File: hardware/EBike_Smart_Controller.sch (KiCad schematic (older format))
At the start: 18 parts

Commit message: More work on schematic: added connections to Zero LPC2103 board.
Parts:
- added P3: Zero LPC2103 board, symbol CONN_20X2
- added P4: BLUETOOTH_MODULE, symbol BLUETOOTH_MODULE
- C1, C3, C4: renamed from C?; value 100nF -> 10nF
- gave numbers to parts that had none: 15
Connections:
- net labels added: UART RX (LPC2103 P0.1), UART TX (LPC2103 P0.0)
- wire segments 63 -> 71
- no-connect marks 0 -> 59
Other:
- note added: "ERROR: needs conversion from 5V to 3.3V!!"

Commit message: This may be a final version of the schematic.
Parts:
- added P5, P6: CONN_10, symbol CONN_10
- added R11: 2K2, symbol R_MINI
- added R12, R13, R14, R15, R16, R17: 3K6, symbol R_MINI
- R10, R8, R9: value 10K -> 2K2
- R2, R4: value 3K6 -> 3K6 1%
- R3, R5: value 6K8 -> 6K8 1%
- R6: value 100K -> 100K 1%
- R7: value 10K -> 10K 1%
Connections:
- net labels added: IO for mosfet phase_a low (LPC2103 P0.7), IO for mosfet phase_b low (LPC2103 P0.8), IO for mosfet phase_c low (LPC2103 P0.9), PWM for mosfet phase_a high (LPC2103 P0.12), PWM for mosfet phase_b high (LPC2103 P0.13), PWM for mosfet phase_c high (LPC2103 P0.19)
- wire segments 71 -> 123
- no-connect marks 59 -> 55
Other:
- note added: "(C28)"
- note added: "(CPU1)"
- note added: "(CPU2)"
- note added: "(CPU3)"
- note added: "(CPU32)"
- note added: "(CPU33)"
- note added: "(CPU4)"
- note added: "(CPU44)"
- note added: "(CPU5)"
- note added: "(R50)"
- note added: "(R55)"
- note added: "(R56)"
- note added: "EBike Smart Controller main board"
- note added: "KU63 controller"
- note added: "Note: 3V3 power\nsource is from\nZero LPC2103\nboard."
- note added: "Note: 5V power source is from KU63 controller."
- note added: "Note: LPC2103 pins are 5V tolerant."
- note added: "Note: exchange R46 (shunt resistor) by this current sensor IC."
- note added: "Note: please refer to KU63 schematic."
- note added: "Zero LPC2103 board"
- note removed: "ERROR: needs conversion from 5V to 3.3V!!"
- moved on the sheet: C1, C2, C3, C4, IC1, K1, P1, P2, R1, R10, R2, R3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

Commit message: Small updates to schematic.
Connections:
- wire segments 123 -> 117
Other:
- note added: "solder to LPC2103 board Vcc input"
- moved on the sheet: K1, P2

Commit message: Added capacitor to schematic, for filtering/average the current signal.
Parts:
- added C5: 100nF, symbol C_MINI
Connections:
- net labels added: IO for mosfet phase_a high (LPC2103 P0.7), IO for mosfet phase_b high (LPC2103 P0.8), IO for mosfet phase_c high (LPC2103 P0.9), PWM for mosfet phase_a low (LPC2103 P0.12), PWM for mosfet phase_b low (LPC2103 P0.13), PWM for mosfet phase_c low (LPC2103 P0.19)
- net labels removed: IO for mosfet phase_a low (LPC2103 P0.7), IO for mosfet phase_b low (LPC2103 P0.8), IO for mosfet phase_c low (LPC2103 P0.9), PWM for mosfet phase_a high (LPC2103 P0.12), PWM for mosfet phase_b high (LPC2103 P0.13), PWM for mosfet phase_c high (LPC2103 P0.19)
- wire segments 117 -> 118
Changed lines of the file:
@@
-EESchema Schematic File Version 2  date Sáb 27 Out 2012 18:03:45 WEST
+EESchema Schematic File Version 2  date Qui 15 Nov 2012 23:12:05 WET
 LIBS:Allegro_ACS754_ACS755_ACS756_HallCurrentSensor_RevA
 LIBS:ac-dc
@@
 Sheet 1 1
 Title "EBike Smart Controller"
-Date "27 oct 2012"
+Date "15 nov 2012"
 Rev "V0.1"
 Comp "Author: Jorge Pinto aka Casainho (casainho@gmail.com)"
@@
 Comment4 ""
 $EndDescr
+Connection ~ 3450 4050
+$Comp
+L GND #PWR8
+U 1 1 50A57363
+P 3450 4400
+F 0 "#PWR8" H 3450 4400 30  0001 C CNN
+F 1 "GND" H 3450 4330 30  0001 C CNN
+	1    3450 4400
+	1    0    0    -1
+$EndComp
+$Comp
+L C_MINI C5
+U 1 1 50A57362
+P 3450 4150
+F 0 "C5" V 3400 4190 30  0000 C CNN
+F 1 "100nF" V 3500 4220 25  0000 C CNN
+	1    3450 4150
+	0    -1   -1   0
+$EndComp
+Wire Wire Line
+	3450 4400 3450 4250
 Text Notes 12150 7550 0    60   ~ 0
 solder to LPC2103 board Vcc input
@@
 	8900 7600 14500 7600
 $Comp
-L +5V #PWR?
+L +5V #PWR26
 U 1 1 508C1378
 P 12000 7500
-F 0 "#PWR?" H 12000 7590 20  0001 C CNN
+F 0 "#PWR26" H 12000 7590 20  0001 C CNN
 F 1 "+5V" H 12000 7590 30  0000 C CNN
 	1    12000 7500
@@
 $EndComp
 $Comp
-L +5V #PWR8
+L +5V #PWR9
 U 1 1 5084124F
 P 4000 6700
-F 0 "#PWR8" H 4000 6790 20  0001 C CNN
+F 0 "#PWR9" H 4000 6790 20  0001 C CNN
 F 1 "+5V" H 4000 6790 30  0000 C CNN
 	1    4000 6700
@@
 $EndComp
 $Comp
-L GND #PWR?
+L GND #PWR13
 U 1 1 508C12D8
 P 6450 3400
-F 0 "#PWR?" H 6450 3400 30  0001 C CNN
+F 0 "#PWR13" H 6450 3400 30  0001 C CNN
 F 1 "GND" H 6450 3330 30  0001 C CNN
 	1    6450 3400
@@
 $EndComp
 $Comp
-L GND #PWR?
+L GND #PWR14
 U 1 1 508C1271
 P 6450 4600
-F 0 "#PWR?" H 6450 4600 30  0001 C CNN
+F 0 "#PWR14" H 6450 4600 30  0001 C CNN
 F 1 "GND" H 6450 4530 30  0001 C CNN
 	1    6450 4600
@@
 $EndComp
 Text Label 11200 6100 2    60   ~ 0
-PWM for mosfet phase_a high (LPC2103 P0.12)
+PWM for mosfet phase_a low (LPC2103 P0.12)
 Text Label 14450 6100 2    60   ~ 0
-PWM for mosfet phase_b high (LPC2103 P0.13)
+PWM for mosfet phase_b low (LPC2103 P0.13)
 NoConn ~ 11350 6600
 Text Label 11200 6600 2    60   ~ 0
-PWM for mosfet phase_c high (LPC2103 P0.19)
+PWM for mosfet phase_c low (LPC2103 P0.19)
 Text Label 8300 6900 2    60   ~ 0
-IO for mosfet phase_a low (LPC2103 P0.7)
+IO for mosfet phase_a high (LPC2103 P0.7)
 Text Label 11200 5900 2    60   ~ 0
-IO for mosfet phase_b low (LPC2103 P0.8)
+IO for mosfet phase_b high (LPC2103 P0.8)
 Text Label 14250 5900 2    60   ~ 0
-IO for mosfet phase_c low (LPC2103 P0.9)
+IO for mosfet phase_c high (LPC2103 P0.9)
 Text Notes 3800 6800 2    50   ~ 0
 Note: 5V power source is from KU63 controller.
@@
 Zero LPC2103 board
 Text Label 8500 7200 2    60   ~ 0
-PWM for mosfet phase_a high (LPC2103 P0.12)
+PWM for mosfet phase_a low (LPC2103 P0.12)
 Text Label 8500 7000 2    60   ~ 0
-PWM for mosfet phase_c high (LPC2103 P0.19)
+PWM for mosfet phase_c low (LPC2103 P0.19)
 Text Label 8300 6800 2    60   ~ 0
-IO for mosfet phase_b low (LPC2103 P0.8)
+IO for mosfet phase_b high (LPC2103 P0.8)
 Text Label 8300 6700 2    60   ~ 0
-IO for mosfet phase_c low (LPC2103 P0.9)
-$Comp
-L +5V #PWR19
+IO for mosfet phase_c high (LPC2103 P0.9)
+$Comp
+L +5V #PWR18
 U 1 1 50846743
 P 6550 6600
-F 0 "#PWR19" H 6550 6690 20  0001 C CNN
+F 0 "#PWR18" H 6550 6690 20  0001 C CNN
 F 1 "+5V" H 6550 6690 30  0000 C CNN
 	1    6550 6600
@@
 $EndComp
 $Comp
-L GND #PWR16
+L GND #PWR17
 U 1 1 50846742
 P 6450 6350
-F 0 "#PWR16" H 6450 6350 30  0001 C CNN
+F 0 "#PWR17" H 6450 6350 30  0001 C CNN
 F 1 "GND" H 6450 6280 30  0001 C CNN
 	1    6450 6350
@@
 $EndComp
 Text Label 14250 5800 2    60   ~ 0
-IO for mosfet phase_a low (LPC2103 P0.7)
+IO for mosfet phase_a high (LPC2103 P0.7)
 Text Label 8500 7100 2    60   ~ 0
-PWM for mosfet phase_b high (LPC2103 P0.13)
+PWM for mosfet phase_b low (LPC2103 P0.13)
 Text Label 7800 7300 2    60   ~ 0
 Current_signal (LPC2103 P0.23)
@@
 Current_signal (LPC2103 P0.23)
 Text Label 2050 6200 0    60   ~ 0
-PWM for mosfet phase_b high (LPC2103 P0.13)
+PWM for mosfet phase_b low (LPC2103 P0.13)
 Text Label 2250 6400 0    60   ~ 0
-IO for mosfet phase_a low (LPC2103 P0.7)
-$Comp
-L GND #PWR9
+IO for mosfet phase_a high (LPC2103 P0.7)
+$Comp
+L GND #PWR10
 U 1 1 50841255
 P 4100 6950
-F 0 "#PWR9" H 4100 6950 30  0001 C CNN
+F 0 "#PWR10" H 4100 6950 30  0001 C CNN
 F 1 "GND" H 4100 6880 30  0001 C CNN
 	1    4100 6950
@@
 $EndComp
 Text Label 2250 6600 0    60   ~ 0
-IO for mosfet phase_c low (LPC2103 P0.9)
+IO for mosfet phase_c high (LPC2103 P0.9)
 Text Label 2250 6500 0    60   ~ 0
-IO for mosfet phase_b low (LPC2103 P0.8)
+IO for mosfet phase_b high (LPC2103 P0.8)
 Text Label 2050 6300 0    60   ~ 0
-PWM for mosfet phase_c high (LPC2103 P0.19)
+PWM for mosfet phase_c low (LPC2103 P0.19)
 Text Label 2050 6100 0    60   ~ 0
-PWM for mosfet phase_a high (LPC2103 P0.12)
+PWM for mosfet phase_a low (LPC2103 P0.12)
 Text Label 3350 4050 0    60   ~ 0
 Current_signal (LPC2103 P0.23)
@@
 KU63 controller
 $Comp
-L +5V #PWR22
+L +5V #PWR23
 U 1 1 508410D2
 P 7150 2450
-F 0 "#PWR22" H 7150 2540 20  0001 C CNN
+F 0 "#PWR23" H 7150 2540 20  0001 C CNN
 F 1 "+5V" H 7150 2540 30  0000 C CNN
 	1    7150 2450
@@
 $EndComp
 $Comp
-L +5V #PWR21
+L +5V #PWR22
 U 1 1 508410CE
 P 6900 2450
-F 0 "#PWR21" H 6900 2540 20  0001 C CNN
+F 0 "#PWR22" H 6900 2540 20  0001 C CNN
 F 1 "+5V" H 6900 2540 30  0000 C CNN
 	1    6900 2450
@@
 $EndComp
 $Comp
-L +5V #PWR17
+L +5V #PWR19
 U 1 1 508410CC
 P 6650 2450
-F 0 "#PWR17" H 6650 2540 20  0001 C CNN
+F 0 "#PWR19" H 6650 2540 20  0001 C CNN
 F 1 "+5V" H 6650 2540 30  0000 C CNN
 	1    6650 2450
@@
 Current_signal (LPC2103 P0.23)
 $Comp
-L +3.3V #PWR26
+L +3.3V #PWR28
 U 1 1 5083CE03
 P 12350 7300
-F 0 "#PWR26" H 12350 7260 30  0001 C CNN
+F 0 "#PWR28" H 12350 7260 30  0001 C CNN
 F 1 "+3.3V" H 12350 7410 30  0000 C CNN
 	1    12350 7300
@@
 $EndComp
 $Comp
-L GND #PWR25
+L GND #PWR27
 U 1 1 5083CDAD
 P 12350 6550
-F 0 "#PWR25" H 12350 6550 30  0001 C CNN
+F 0 "#PWR27" H 12350 6550 30  0001 C CNN
 F 1 "GND" H 12350 6480 30  0001 C CNN
 	1    12350 6550
@@
 UART RX (LPC2103 P0.1)
 $Comp
-L +3.3V #PWR23
+L +3.3V #PWR24
 U 1 1 5083C9AC
 P 11650 3850
-F 0 "#PWR23" H 11650 3810 30  0001 C CNN
+F 0 "#PWR24" H 11650 3810 30  0001 C CNN
 F 1 "+3.3V" H 11650 3960 30  0000 C CNN
 	1    11650 3850
@@
 $EndComp
 $Comp
-L GND #PWR24
+L GND #PWR25
 U 1 1 5083C9A1
 P 11650 4200
-F 0 "#PWR24" H 11650 4200 30  0001 C CNN
+F 0 "#PWR25" H 11650 4200 30  0001 C CNN
 F 1 "GND" H 11650 4130 30  0001 C CNN
 	1    11650 4200
@@
 $EndComp
 $Comp
-L +3.3V #PWR14
+L +3.3V #PWR15
 U 1 1 5083200B
 P 6450 5150
-F 0 "#PWR14" H 6450 5110 30  0001 C CNN
+F 0 "#PWR15" H 6450 5110 30  0001 C CNN
 F 1 "+3.3V" H 6450 5260 30  0000 C CNN
 	1    6450 5150
@@
 $EndComp
 $Comp
-L GND #PWR15
+L GND #PWR16
 U 1 1 50831F3E
 P 6450 5850
-F 0 "#PWR15" H 6450 5850 30  0001 C CNN
+F 0 "#PWR16" H 6450 5850 30  0001 C CNN
 F 1 "GND" H 6450 5780 30  0001 C CNN
 	1    6450 5850
@@
 $EndComp
 $Comp
-L GND #PWR20
+L GND #PWR21
 U 1 1 50831E6E
 P 6850 4600
-F 0 "#PWR20" H 6850 4600 30  0001 C CNN
+F 0 "#PWR21" H 6850 4600 30  0001 C CNN
 F 1 "GND" H 6850 4530 30  0001 C CNN
 	1    6850 4600
@@
 $EndComp
 $Comp
-L +5V #PWR10
+L +5V #PWR12
 U 1 1 50831D0B
 P 6400 4050
-F 0 "#PWR10" H 6400 4140 20  0001 C CNN
+F 0 "#PWR12" H 6400 4140 20  0001 C CNN
 F 1 "+5V" H 6400 4140 30  0000 C CNN
 	1    6400 4050
@@
 $EndComp
 $Comp
-L GND #PWR18
+L GND #PWR20
 U 1 1 50831D04
 P 6650 4600
-F 0 "#PWR18" H 6650 4600 30  0001 C CNN
+F 0 "#PWR20" H 6650 4600 30  0001 C CNN
 F 1 "GND" H 6650 4530 30  0001 C CNN
 	1    6650 4600

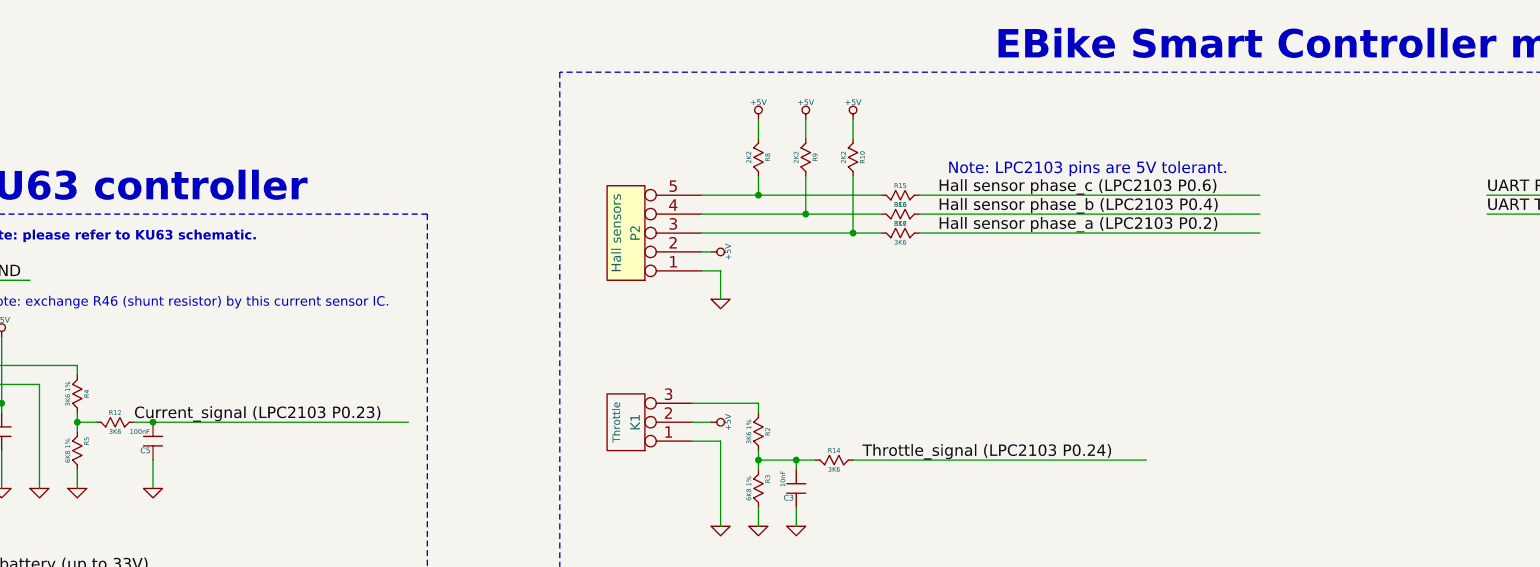
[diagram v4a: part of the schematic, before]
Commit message: Added 10nF capacitors to Hall Sensors line signals. Now the firmware works better!
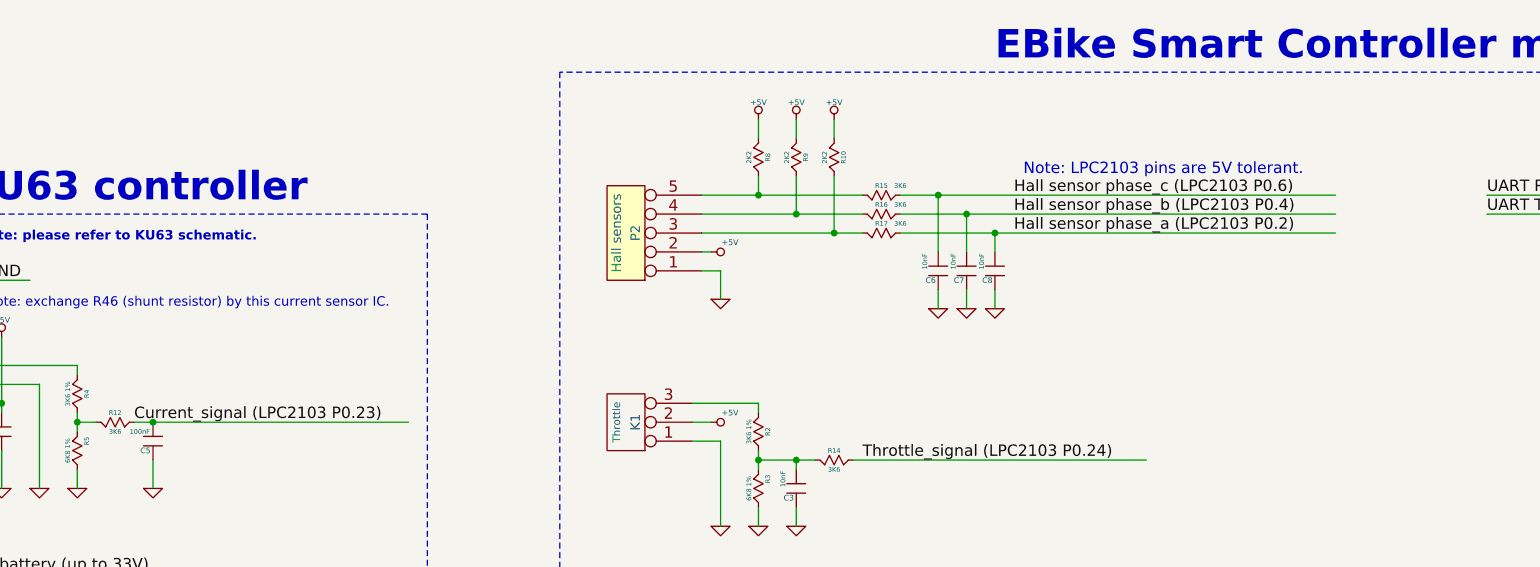
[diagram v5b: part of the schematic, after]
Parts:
- added C6, C7, C8: 10nF, symbol C_MINI
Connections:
- wire segments 118 -> 128
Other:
- moved on the sheet: R10, R15, R16, R17, R9

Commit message: Added resistors for pull ups and pull downs.
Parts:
- added R? (x3): 10k, symbol R_MINI
- added R? (x3): 10K, symbol R_MINI
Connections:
- wire segments 128 -> 124
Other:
- moved on the sheet: C1, C3, C6, C7, C8, K1, P1, P2, R1, R10, R13, R14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

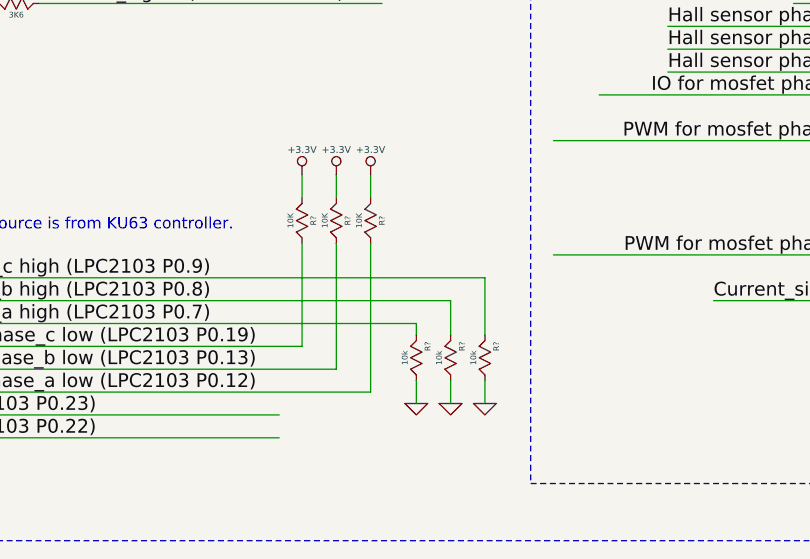
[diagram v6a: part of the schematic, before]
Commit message: Schematic update, for some pull up and pull down resistors.
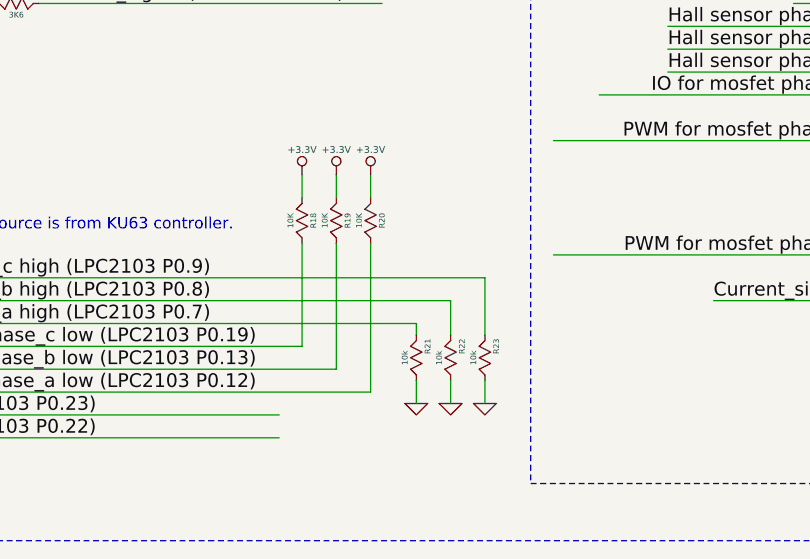
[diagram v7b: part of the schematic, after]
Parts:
- gave numbers to parts that had none: 6
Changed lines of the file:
@@
-EESchema Schematic File Version 2  date Qui 06 Dez 2012 22:49:30 WET
+EESchema Schematic File Version 2  date Seg 10 Dez 2012 11:00:59 WET
 LIBS:Allegro_ACS754_ACS755_ACS756_HallCurrentSensor_RevA
 LIBS:ac-dc
@@
 Sheet 1 1
 Title "EBike Smart Controller"
-Date "6 dec 2012"
+Date "10 dec 2012"
 Rev "V0.1"
 Comp "Author: Jorge Pinto aka Casainho (casainho@gmail.com)"
@@
 	8650 7200 5950 7200
 $Comp
-L R_MINI R?
+L R_MINI R20
 U 1 1 50BE831C
 P 8650 6450
-F 0 "R?" H 8650 6400 25  0000 C CNN
+F 0 "R20" H 8650 6400 25  0000 C CNN
 F 1 "10K" H 8650 6500 25  0000 C CNN
 	1    8650 6450
@@
 $EndComp
 $Comp
-L +3.3V #PWR?
+L +3.3V #PWR29
 U 1 1 50BE831B
 P 8650 6250
-F 0 "#PWR?" H 8650 6210 30  0001 C CNN
+F 0 "#PWR29" H 8650 6210 30  0001 C CNN
 F 1 "+3.3V" H 8650 6360 30  0000 C CNN
 	1    8650 6250
@@
 $EndComp
 $Comp
-L +3.3V #PWR?
+L +3.3V #PWR28
 U 1 1 50BE82D1
 P 8500 6250
-F 0 "#PWR?" H 8500 6210 30  0001 C CNN
+F 0 "#PWR28" H 8500 6210 30  0001 C CNN
 F 1 "+3.3V" H 8500 6360 30  0000 C CNN
 	1    8500 6250
@@
 $EndComp
 $Comp
-L R_MINI R?
+L R_MINI R19
 U 1 1 50BE82D0
 P 8500 6450
-F 0 "R?" H 8500 6400 25  0000 C CNN
+F 0 "R19" H 8500 6400 25  0000 C CNN
 F 1 "10K" H 8500 6500 25  0000 C CNN
 	1    8500 6450
@@
 $EndComp
 $Comp
-L R_MINI R?
+L R_MINI R18
 U 1 1 50BE82C6
 P 8350 6450
-F 0 "R?" H 8350 6400 25  0000 C CNN
+F 0 "R18" H 8350 6400 25  0000 C CNN
 F 1 "10K" H 8350 6500 25  0000 C CNN
 	1    8350 6450
@@
 $EndComp
 $Comp
-L +3.3V #PWR?
+L +3.3V #PWR27
 U 1 1 50BE82C5
 P 8350 6250
-F 0 "#PWR?" H 8350 6210 30  0001 C CNN
+F 0 "#PWR27" H 8350 6210 30  0001 C CNN
 F 1 "+3.3V" H 8350 6360 30  0000 C CNN
 	1    8350 6250
@@
 $EndComp
 $Comp
-L GND #PWR?
+L GND #PWR32
 U 1 1 50BE8296
 P 9150 7250
-F 0 "#PWR?" H 9150 7250 30  0001 C CNN
+F 0 "#PWR32" H 9150 7250 30  0001 C CNN
 F 1 "GND" H 9150 7180 30  0001 C CNN
 	1    9150 7250
@@
 $EndComp
 $Comp
-L R_MINI R?
+L R_MINI R23
 U 1 1 50BE8295
 P 9150 7050
-F 0 "R?" H 9200 7000 25  0000 C CNN
+F 0 "R23" H 9200 7000 25  0000 C CNN
 F 1 "10k" H 9150 7100 25  0000 C CNN
 	1    9150 7050
@@
 $EndComp
 $Comp
-L R_MINI R?
+L R_MINI R22
 U 1 1 50BE828D
 P 9000 7050
-F 0 "R?" H 9050 7000 25  0000 C CNN
+F 0 "R22" H 9050 7000 25  0000 C CNN
 F 1 "10k" H 9000 7100 25  0000 C CNN
 	1    9000 7050
@@
 $EndComp
 $Comp
-L GND #PWR?
+L GND #PWR31
 U 1 1 50BE828C
 P 9000 7250
-F 0 "#PWR?" H 9000 7250 30  0001 C CNN
+F 0 "#PWR31" H 9000 7250 30  0001 C CNN
 F 1 "GND" H 9000 7180 30  0001 C CNN
 	1    9000 7250
@@
 $EndComp
 $Comp
-L GND #PWR?
+L GND #PWR30
 U 1 1 50BE8164
 P 8850 7250
-F 0 "#PWR?" H 8850 7250 30  0001 C CNN
+F 0 "#PWR30" H 8850 7250 30  0001 C CNN
 F 1 "GND" H 8850 7180 30  0001 C CNN
 	1    8850 7250
@@
 $EndComp
 $Comp
-L R_MINI R?
+L R_MINI R21
 U 1 1 50BE8163
 P 8850 7050
-F 0 "R?" H 8900 7000 25  0000 C CNN
+F 0 "R21" H 8900 7000 25  0000 C CNN
 F 1 "10k" H 8850 7100 25  0000 C CNN
 	1    8850 7050
@@
 solder to LPC2103 board Vcc input
 $Comp
-L +5V #PWR29
+L +5V #PWR35
 U 1 1 508C1378
 P 12450 7500
-F 0 "#PWR29" H 12450 7590 20  0001 C CNN
+F 0 "#PWR35" H 12450 7590 20  0001 C CNN
 F 1 "+5V" H 12450 7590 30  0000 C CNN
 	1    12450 7500
@@
 $EndComp
 $Comp
-L GND #PWR13
+L GND #PWR15
 U 1 1 508C12D8
 P 6900 3400
-F 0 "#PWR13" H 6900 3400 30  0001 C CNN
+F 0 "#PWR15" H 6900 3400 30  0001 C CNN
 F 1 "GND" H 6900 3330 30  0001 C CNN
 	1    6900 3400
@@
 $EndComp
 $Comp
-L GND #PWR14
+L GND #PWR16
 U 1 1 508C1271
 P 6900 4600
-F 0 "#PWR14" H 6900 4600 30  0001 C CNN
+F 0 "#PWR16" H 6900 4600 30  0001 C CNN
 F 1 "GND" H 6900 4530 30  0001 C CNN
 	1    6900 4600
@@
 IO for mosfet phase_c high (LPC2103 P0.9)
 $Comp
-L +5V #PWR18
+L +5V #PWR12
 U 1 1 50846743
 P 6200 6600
-F 0 "#PWR18" H 6200 6690 20  0001 C CNN
+F 0 "#PWR12" H 6200 6690 20  0001 C CNN
 F 1 "+5V" H 6200 6690 30  0000 C CNN
 	1    6200 6600
@@
 $EndComp
 $Comp
-L GND #PWR17
+L GND #PWR11
 U 1 1 50846742
 P 6100 6350
-F 0 "#PWR17" H 6100 6350 30  0001 C CNN
+F 0 "#PWR11" H 6100 6350 30  0001 C CNN
 F 1 "GND" H 6100 6280 30  0001 C CNN
 	1    6100 6350
@@
 Current_signal (LPC2103 P0.23)
 $Comp
-L +3.3V #PWR31
+L +3.3V #PWR37
 U 1 1 5083CE03
 P 12800 7300
-F 0 "#PWR31" H 12800 7260 30  0001 C CNN
+F 0 "#PWR37" H 12800 7260 30  0001 C CNN
 F 1 "+3.3V" H 12800 7410 30  0000 C CNN
 	1    12800 7300
@@
 $EndComp
 $Comp
-L GND #PWR30
+L GND #PWR36
 U 1 1 5083CDAD
 P 12800 6550
-F 0 "#PWR30" H 12800 6550 30  0001 C CNN
+F 0 "#PWR36" H 12800 6550 30  0001 C CNN
 F 1 "GND" H 12800 6480 30  0001 C CNN
 	1    12800 6550
@@
 UART RX (LPC2103 P0.1)
 $Comp
-L +3.3V #PWR27
+L +3.3V #PWR33
 U 1 1 5083C9AC
 P 12100 3850
-F 0 "#PWR27" H 12100 3810 30  0001 C CNN
+F 0 "#PWR33" H 12100 3810 30  0001 C CNN
 F 1 "+3.3V" H 12100 3960 30  0000 C CNN
 	1    12100 3850
@@
 $EndComp
 $Comp
-L GND #PWR28
+L GND #PWR34
 U 1 1 5083C9A1
 P 12100 4200
-F 0 "#PWR28" H 12100 4200 30  0001 C CNN
+F 0 "#PWR34" H 12100 4200 30  0001 C CNN
 F 1 "GND" H 12100 4130 30  0001 C CNN
 	1    12100 4200
@@
 $EndComp
 $Comp
-L +5V #PWR11
+L +5V #PWR13
 U 1 1 50832572
 P 6850 3150
-F 0 "#PWR11" H 6850 3240 20  0001 C CNN
+F 0 "#PWR13" H 6850 3240 20  0001 C CNN
 F 1 "+5V" V 6800 3250 30  0000 C CNN
 	1    6850 3150
@@
 $EndComp
 $Comp
-L +3.3V #PWR15
+L +3.3V #PWR17
 U 1 1 5083200B
 P 6900 5150
-F 0 "#PWR15" H 6900 5110 30  0001 C CNN
+F 0 "#PWR17" H 6900 5110 30  0001 C CNN
 F 1 "+3.3V" H 6900 5260 30  0000 C CNN
 	1    6900 5150
@@
 $EndComp
 $Comp
-L GND #PWR16
+L GND #PWR18
 U 1 1 50831F3E
 P 6900 5850
-F 0 "#PWR16" H 6900 5850 30  0001 C CNN
+F 0 "#PWR18" H 6900 5850 30  0001 C CNN
 F 1 "GND" H 6900 5780 30  0001 C CNN
 	1    6900 5850
@@
 $EndComp
 $Comp
-L +5V #PWR12
+L +5V #PWR14
 U 1 1 50831D0B
 P 6850 4050
-F 0 "#PWR12" H 6850 4140 20  0001 C CNN
+F 0 "#PWR14" H 6850 4140 20  0001 C CNN
 F 1 "+5V" V 6800 4150 30  0000 C CNN
 	1    6850 4050
